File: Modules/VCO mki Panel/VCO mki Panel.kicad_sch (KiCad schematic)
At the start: 0 parts

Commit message: VCO mki in progress
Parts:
- added H1, H2, H3, H4: MountingHole_Rails, SynthStuff:MountingHole_3.2mm_M3_Pad4mm, symbol SynthStuff:MountingHole_Rails
- added H10: FM Lin, SynthStuff:Pot_Cutout_Tiny, symbol SynthStuff:MountingHole_Pot
- added H11: PWM Mod, SynthStuff:Pot_Cutout_Tiny, symbol SynthStuff:MountingHole_Pot
- added H12: Shape Mod, SynthStuff:Pot_Cutout_Tiny, symbol SynthStuff:MountingHole_Pot
- added H13: Sin, SynthStuff:Jack_6.35mm_Cutout_Output_v5, symbol SynthStuff:MountingHole_Jack6.35mm_Output_v2
- added H14: Tri, SynthStuff:Jack_6.35mm_Cutout_Output_v5, symbol SynthStuff:MountingHole_Jack6.35mm_Output_v2
- added H15: Sqr, SynthStuff:Jack_6.35mm_Cutout_Output_v5, symbol SynthStuff:MountingHole_Jack6.35mm_Output_v2
- added H16: Saw/Var, SynthStuff:Jack_6.35mm_Cutout_Output_v5, symbol SynthStuff:MountingHole_Jack6.35mm_Output_v2
- added H17: CV 1, SynthStuff:Jack_6.35mm_Cutout_v2, symbol SynthStuff:MountingHole_Jack6.35mm_v2
- added H18: CV 2, SynthStuff:Jack_6.35mm_Cutout_v2, symbol SynthStuff:MountingHole_Jack6.35mm_v2
- added H19: PWM CV, SynthStuff:Jack_6.35mm_Cutout_v2, symbol SynthStuff:MountingHole_Jack6.35mm_v2
- added H20: Shape CV, SynthStuff:Jack_6.35mm_Cutout_v2, symbol SynthStuff:MountingHole_Jack6.35mm_v2
- added H21: Calib TrimPot 1, MountingHole:MountingHole_3.2mm_M3, symbol Mechanical:MountingHole
- added H22: Calib TrimPot 2, MountingHole:MountingHole_3.2mm_M3, symbol Mechanical:MountingHole
- added H23: Calib TrimPot 3, MountingHole:MountingHole_3.2mm_M3, symbol Mechanical:MountingHole
- added H24: Sync, SynthStuff:Jack_6.35mm_Cutout_v2, symbol SynthStuff:MountingHole_Jack6.35mm_v2
- added H5: Coarse, SynthStuff:Pot_Cutout_Large, symbol SynthStuff:MountingHole_Pot
- added H6: Shape, SynthStuff:Pot_Cutout_Large, symbol SynthStuff:MountingHole_Pot
- added H7: Fine, SynthStuff:Pot_Cutout_Medium, symbol SynthStuff:MountingHole_Pot
- added H8: PWM, SynthStuff:Pot_Cutout_Medium, symbol SynthStuff:MountingHole_Pot
- added H9: FM Exp, SynthStuff:Pot_Cutout_Tiny, symbol SynthStuff:MountingHole_Pot
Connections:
- new net GND: H1.1, H10.1, H11.1, H12.1, H13.1, H14.1, H15.1, H16.1, H17.1, H18.1, H19.1, H2.1, H20.1, H24.1, H3.1, H4.1, H5.1, H6.1, H7.1, H8.1, H9.1

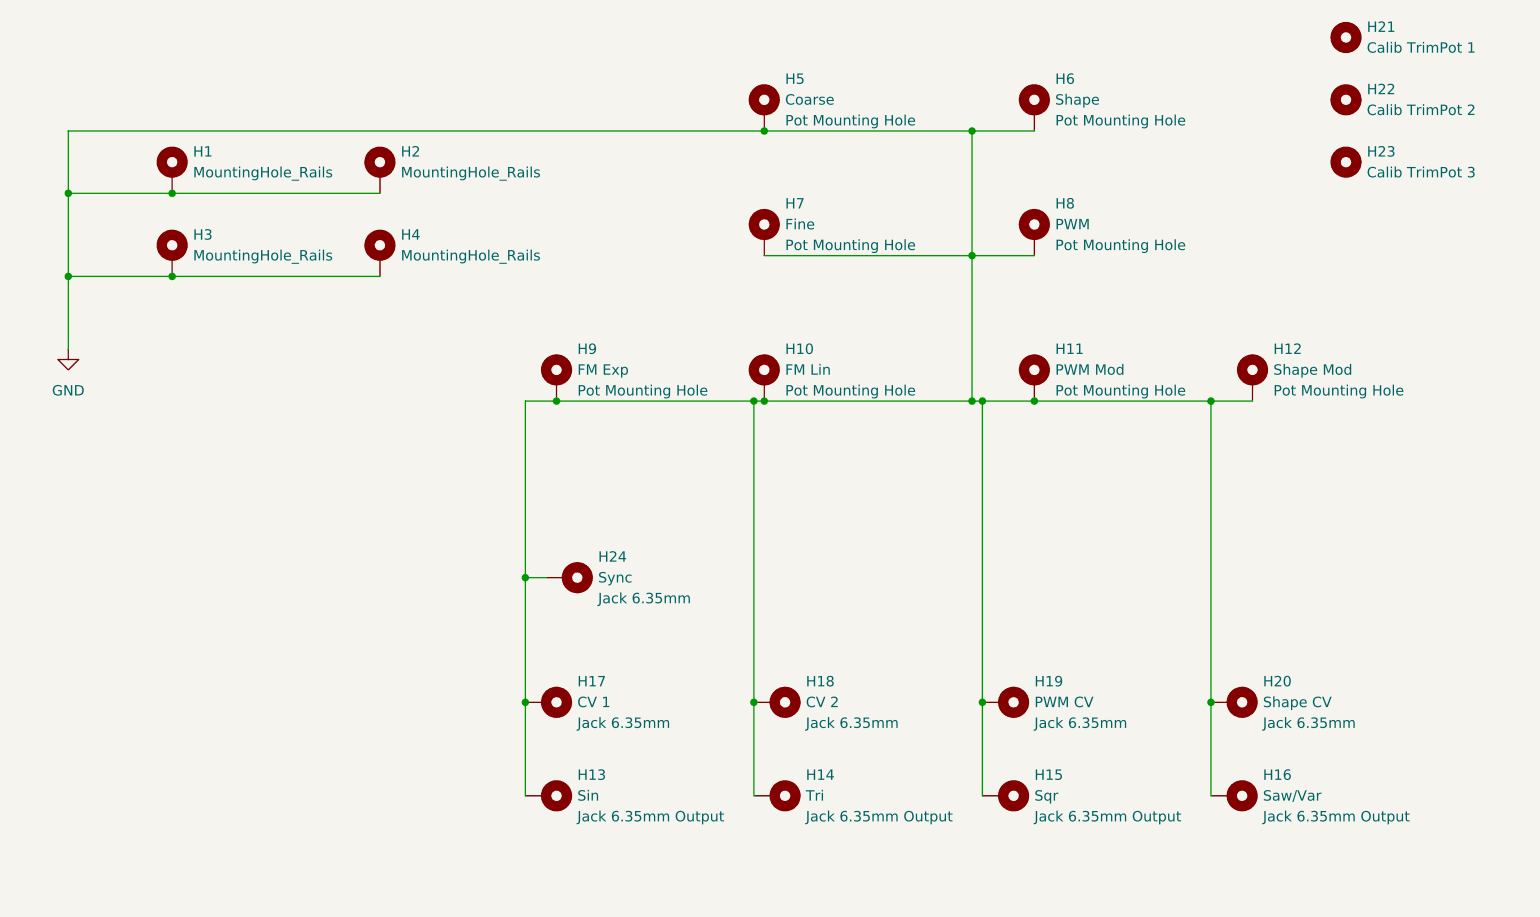
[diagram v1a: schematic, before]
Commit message: Synced SCH to PCB
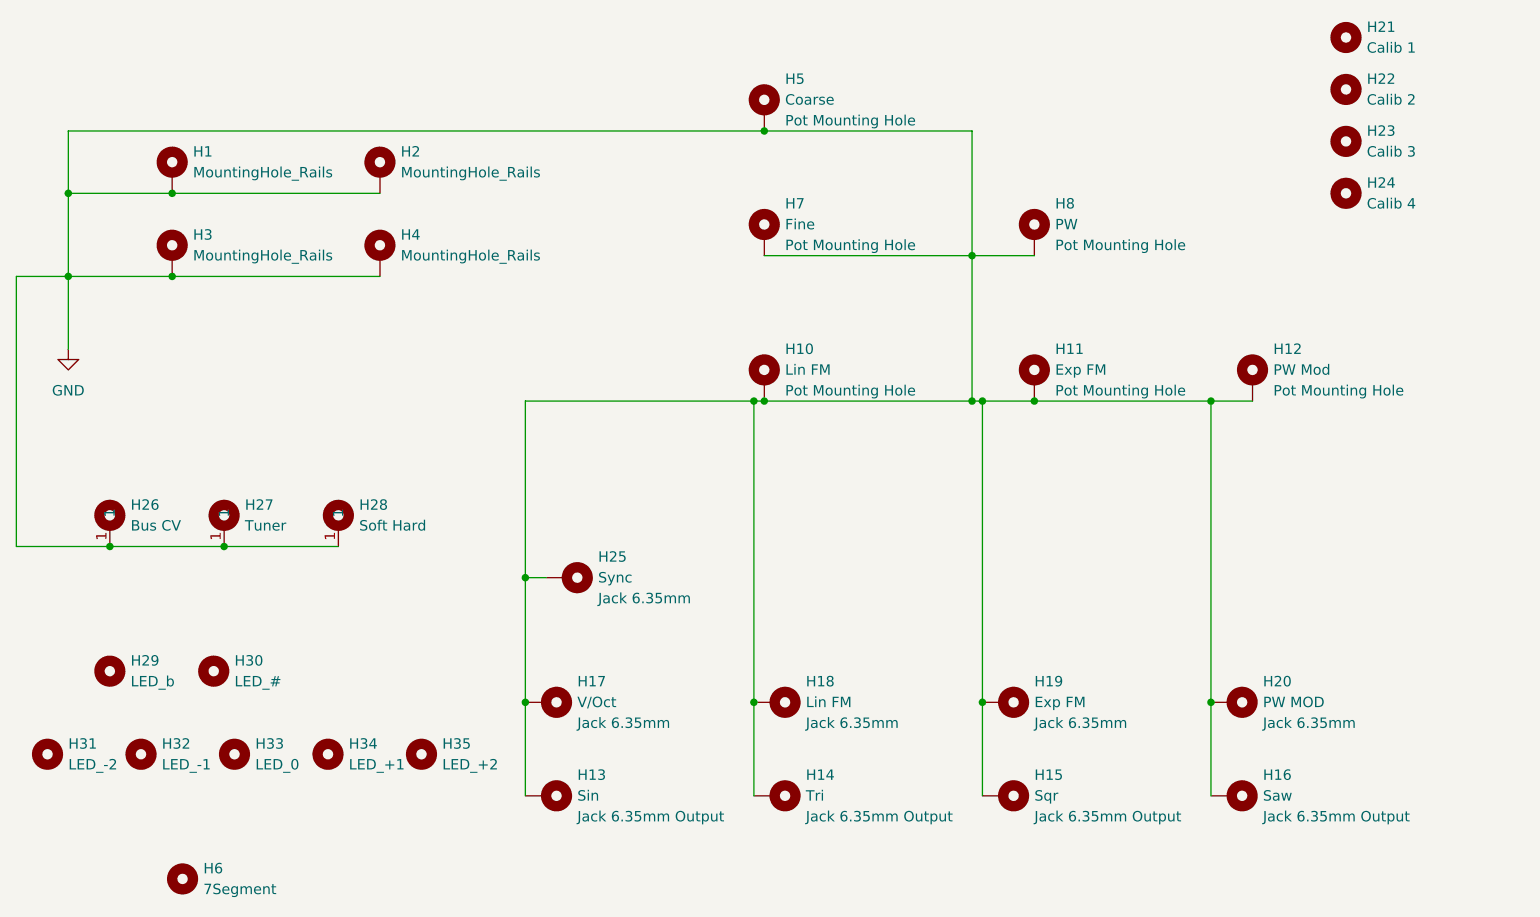
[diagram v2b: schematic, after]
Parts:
- removed H6: Shape, SynthStuff:Pot_Cutout_Large, symbol SynthStuff:MountingHole_Pot
- removed H9: FM Exp, SynthStuff:Pot_Cutout_Tiny, symbol SynthStuff:MountingHole_Pot
- added H23: Calib 3, MountingHole:MountingHole_2.2mm_M2_DIN965, symbol Mechanical:MountingHole
- added H26: Bus CV, SynthStuff:Toggle_Switch_Cutout, symbol SynthStuff:MountingHole_ToggleSwitch
- added H27: Tuner, SynthStuff:Toggle_Switch_Cutout, symbol SynthStuff:MountingHole_ToggleSwitch
- added H28: Soft Hard, SynthStuff:Toggle_Switch_Cutout, symbol SynthStuff:MountingHole_ToggleSwitch
- added H29: LED_b, SynthStuff:MountingHole_LED_3mm, symbol Mechanical:MountingHole
- added H30: LED_#, SynthStuff:MountingHole_LED_3mm, symbol Mechanical:MountingHole
- added H31: LED_-2, SynthStuff:MountingHole_LED_3mm, symbol Mechanical:MountingHole
- added H32: LED_-1, SynthStuff:MountingHole_LED_3mm, symbol Mechanical:MountingHole
- added H33: LED_0, SynthStuff:MountingHole_LED_3mm, symbol Mechanical:MountingHole
- added H34: LED_+1, SynthStuff:MountingHole_LED_3mm, symbol Mechanical:MountingHole
- added H35: LED_+2, SynthStuff:MountingHole_LED_3mm, symbol Mechanical:MountingHole
- added H6: 7Segment, SynthStuff:7Segment_Cutout, symbol Mechanical:MountingHole
- H10: value FM Lin -> Lin FM
- H11: value PWM Mod -> Exp FM
- H12: value Shape Mod -> PW Mod
- H16: value Saw/Var -> Saw
- H17: value CV 1 -> V/Oct
- H18: value CV 2 -> Lin FM
- H19: value PWM CV -> Exp FM
- H20: value Shape CV -> PW MOD
- H21: value Calib TrimPot 1 -> Calib 1; footprint MountingHole:MountingHole_3.2mm_M3 -> MountingHole:MountingHole_2.2mm_M2_DIN965
- H22: value Calib TrimPot 2 -> Calib 2; footprint MountingHole:MountingHole_3.2mm_M3 -> MountingHole:MountingHole_2.2mm_M2_DIN965
- H24: renamed from H23; value Calib TrimPot 3 -> Calib 4; footprint MountingHole:MountingHole_3.2mm_M3 -> MountingHole:MountingHole_2.2mm_M2_DIN965
- H5: footprint SynthStuff:Pot_Cutout_Large -> SynthStuff:Pot_Cutout_Huge_v2; now in the parts list
- H7: footprint SynthStuff:Pot_Cutout_Medium -> SynthStuff:Pot_Cutout_Medium_v2; now in the parts list
- H8: value PWM -> PW; now in the parts list
- renumbered H24 to H25
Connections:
- net GND: now also H26.1, H27.1, H28.1
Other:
- moved on the sheet: H22, H24

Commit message: Updated jack footprints to 12mm washer
... and added hash art to Adapter Mult CV and Gate jacks
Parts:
- H1, H2, H3, H4: footprint SynthStuff:MountingHole_3.2mm_M3_Pad4mm -> SynthStuff:MountingHole_Rails
- H13, H14, H15, H16: footprint SynthStuff:Jack_6.35mm_Cutout_Output_v5 -> SynthStuff:Jack_6.35mm_Cutout_Output_v6
- H17, H18, H19, H20, H25: footprint SynthStuff:Jack_6.35mm_Cutout_v2 -> SynthStuff:Jack_6.35mm_Cutout_v3
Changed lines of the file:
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@@
 			)
 		)
-		(property "Footprint" "SynthStuff:MountingHole_3.2mm_M3_Pad4mm"
+		(property "Footprint" "SynthStuff:MountingHole_Rails"
 			(at 34.29 34.29 0)
 			(effects
@@
 			)
 		)
-		(property "Footprint" "SynthStuff:Jack_6.35mm_Cutout_Output_v5"
+		(property "Footprint" "SynthStuff:Jack_6.35mm_Cutout_Output_v6"
 			(at 137.16 110.49 0)
 			(effects
@@
 			)
 		)
-		(property "Footprint" "SynthStuff:MountingHole_3.2mm_M3_Pad4mm"
+		(property "Footprint" "SynthStuff:MountingHole_Rails"
 			(at 59.69 34.29 0)
 			(effects
@@
 			)
 		)
-		(property "Footprint" "SynthStuff:MountingHole_3.2mm_M3_Pad4mm"
+		(property "Footprint" "SynthStuff:MountingHole_Rails"
 			(at 34.29 44.45 0)
 			(effects
@@
 			)
 		)
-		(property "Footprint" "SynthStuff:Jack_6.35mm_Cutout_Output_v5"
+		(property "Footprint" "SynthStuff:Jack_6.35mm_Cutout_Output_v6"
 			(at 165.1 110.49 0)
 			(effects
@@
 			)
 		)
-		(property "Footprint" "SynthStuff:Jack_6.35mm_Cutout_v2"
+		(property "Footprint" "SynthStuff:Jack_6.35mm_Cutout_v3"
 			(at 81.28 99.06 0)
 			(effects
@@
 			)
 		)
-		(property "Footprint" "SynthStuff:Jack_6.35mm_Cutout_Output_v5"
+		(property "Footprint" "SynthStuff:Jack_6.35mm_Cutout_Output_v6"
 			(at 109.22 110.49 0)
 			(effects
@@
 			)
 		)
-		(property "Footprint" "SynthStuff:Jack_6.35mm_Cutout_v2"
+		(property "Footprint" "SynthStuff:Jack_6.35mm_Cutout_v3"
 			(at 83.82 83.82 0)
 			(effects
@@
 			)
 		)
-		(property "Footprint" "SynthStuff:Jack_6.35mm_Cutout_v2"
+		(property "Footprint" "SynthStuff:Jack_6.35mm_Cutout_v3"
 			(at 137.16 99.06 0)
 			(effects
@@
 			)
 		)
-		(property "Footprint" "SynthStuff:Jack_6.35mm_Cutout_v2"
+		(property "Footprint" "SynthStuff:Jack_6.35mm_Cutout_v3"
 			(at 165.1 99.06 0)
 			(effects
@@
 			)
 		)
-		(property "Footprint" "SynthStuff:Jack_6.35mm_Cutout_v2"
+		(property "Footprint" "SynthStuff:Jack_6.35mm_Cutout_v3"
 			(at 109.22 99.06 0)
 			(effects
@@
 			)
 		)
-		(property "Footprint" "SynthStuff:MountingHole_3.2mm_M3_Pad4mm"
+		(property "Footprint" "SynthStuff:MountingHole_Rails"
 			(at 59.69 44.45 0)
 			(effects
@@
 			)
 		)
-		(property "Footprint" "SynthStuff:Jack_6.35mm_Cutout_Output_v5"
+		(property "Footprint" "SynthStuff:Jack_6.35mm_Cutout_Output_v6"
 			(at 81.28 110.49 0)
 			(effects

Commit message: More adjustments to panel
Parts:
- added J1: GND, Connector_Wire:SolderWirePad_1x01_SMD_5x10mm, symbol Connector_Generic:Conn_01x01
- H8: value PW -> Pulse Width
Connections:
- net GND: now also J1.1 (Pin_1)
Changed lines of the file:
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@@
+	)
+	(junction
+		(at 21.59 53.34)
+		(diameter 0)
+		(color 0 0 0 0)
 	)
 	(junction
@@
 	(wire
 		(pts
+			(xy 21.59 53.34) (xy 21.59 55.88)
+		)
+		(stroke
+			(width 0)
+			(type default)
+		)
+	)
+	(wire
+		(pts
 			(xy 106.68 29.21) (xy 132.08 29.21)
 		)
@@
 	(wire
 		(pts
-			(xy 21.59 46.99) (xy 21.59 55.88)
+			(xy 21.59 46.99) (xy 21.59 53.34)
 		)
 		(stroke
@@
 		(pts
 			(xy 40.64 80.01) (xy 54.61 80.01)
+		)
+		(stroke
+			(width 0)
+			(type default)
+		)
+	)
+	(wire
+		(pts
+			(xy 21.59 53.34) (xy 29.21 53.34)
 		)
 		(stroke
@@
 	)
 	(symbol
+		(lib_id "Connector_Generic:Conn_01x01")
+		(at 34.29 53.34 0)
+		(unit 1)
+		(exclude_from_sim no)
+		(in_bom yes)
+		(on_board yes)
+		(dnp no)
+		(fields_autoplaced yes)
+		(property "Reference" "J1"
+			(at 36.83 52.0699 0)
+			(effects
+				(font
+					(size 1.27 1.27)
+				)
+				(justify left)
+			)
+		)
+		(property "Value" "GND"
+			(at 36.83 54.6099 0)
+			(effects
+				(font
+					(size 1.27 1.27)
+				)
+				(justify left)
+			)
+		)
+		(property "Footprint" "Connector_Wire:SolderWirePad_1x01_SMD_5x10mm"
+			(at 34.29 53.34 0)
+			(effects
+				(font
+					(size 1.27 1.27)
+				)
+				(hide yes)
+			)
+		)
+		(property "Datasheet" "~"
+			(at 34.29 53.34 0)
+			(effects
+				(font
+					(size 1.27 1.27)
+				)
+				(hide yes)
+			)
+		)
+		(property "Description" "Generic connector, single row, 01x01, script generated (kicad-library-utils/schlib/autogen/connector/)"
+			(at 34.29 53.34 0)
+			(effects
+				(font
+					(size 1.27 1.27)
+				)
+				(hide yes)
+			)
+		)
+		(pin "1"
+		)
+		(instances
+			(project ""
+				(path "/1ac843a2-b018-4f05-9c7c-f861332ffc39"
+					(reference "J1")
+					(unit 1)
+				)
+			)
+		)
+	)
+	(symbol
 		(lib_id "SynthStuff:MountingHole_Pot")
 		(at 106.68 26.67 0)
@@
 			)
 		)
-		(property "Value" "PW"
+		(property "Value" "Pulse Width"
 			(at 142.24 40.6399 0)
 			(effects

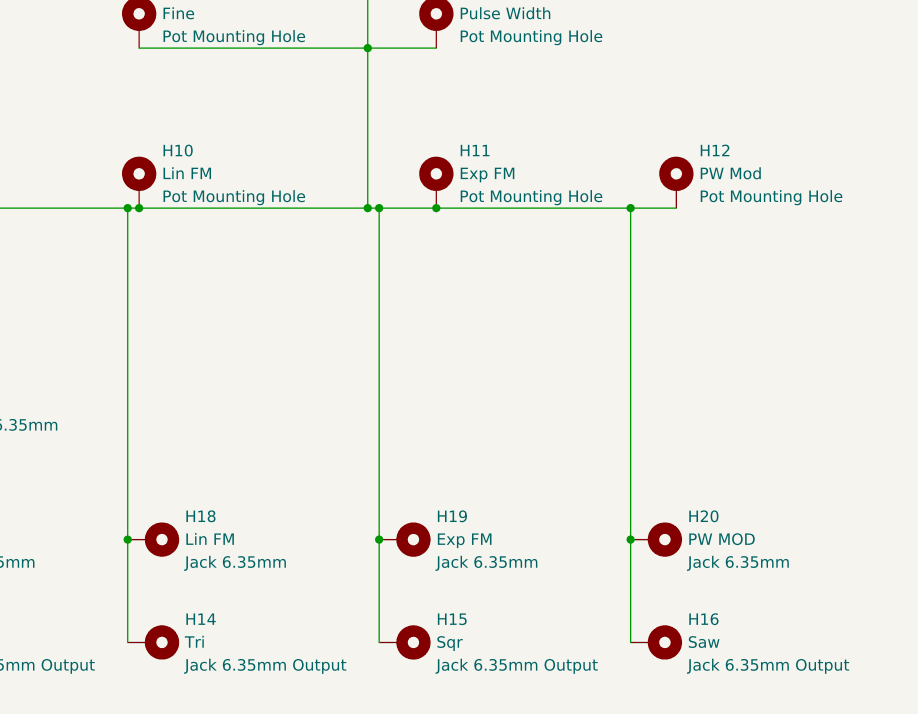
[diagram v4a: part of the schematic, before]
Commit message: Created VCO sub sheets
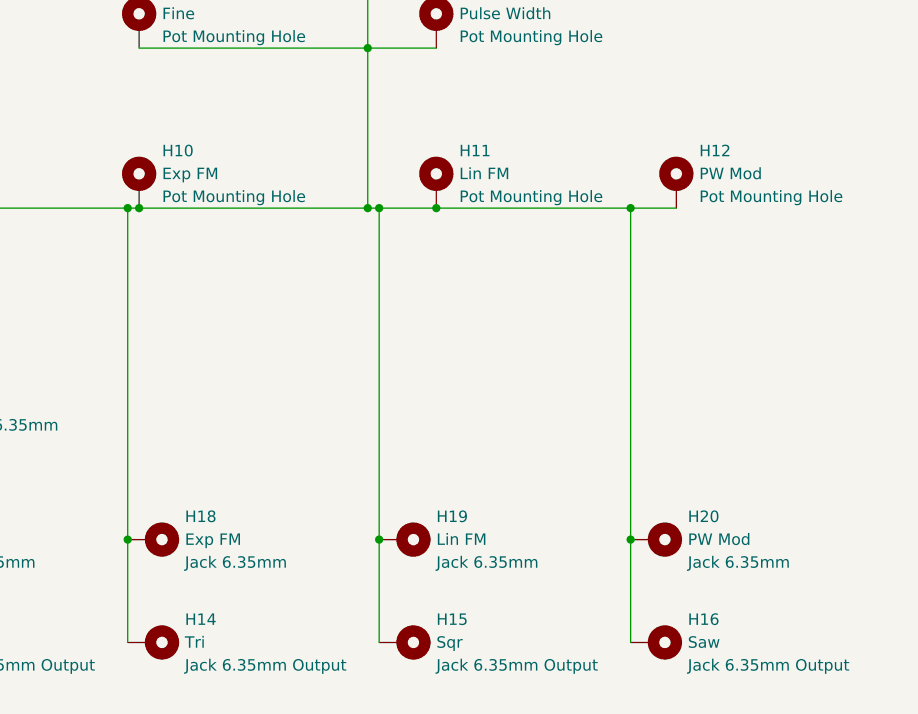
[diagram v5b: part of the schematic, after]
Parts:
- H10, H18: value Lin FM -> Exp FM
- H11, H19: value Exp FM -> Lin FM
- H20: value PW MOD -> PW Mod
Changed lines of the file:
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@@
 			)
 		)
-		(property "Value" "Exp FM"
+		(property "Value" "Lin FM"
 			(at 142.24 58.4199 0)
 			(effects
@@
 			)
 		)
-		(property "Value" "Lin FM"
+		(property "Value" "Exp FM"
 			(at 109.22 58.4199 0)
 			(effects
@@
 			)
 		)
-		(property "Value" "Exp FM"
+		(property "Value" "Lin FM"
 			(at 139.7 99.0599 0)
 			(effects
@@
 			)
 		)
-		(property "Value" "PW MOD"
+		(property "Value" "PW Mod"
 			(at 167.64 99.0599 0)
 			(effects
@@
 			)
 		)
-		(property "Value" "Lin FM"
+		(property "Value" "Exp FM"
 			(at 111.76 99.0599 0)
 			(effects
